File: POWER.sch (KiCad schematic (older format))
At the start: 35 parts, among them U201 TPS61021A, U402 MAX1555

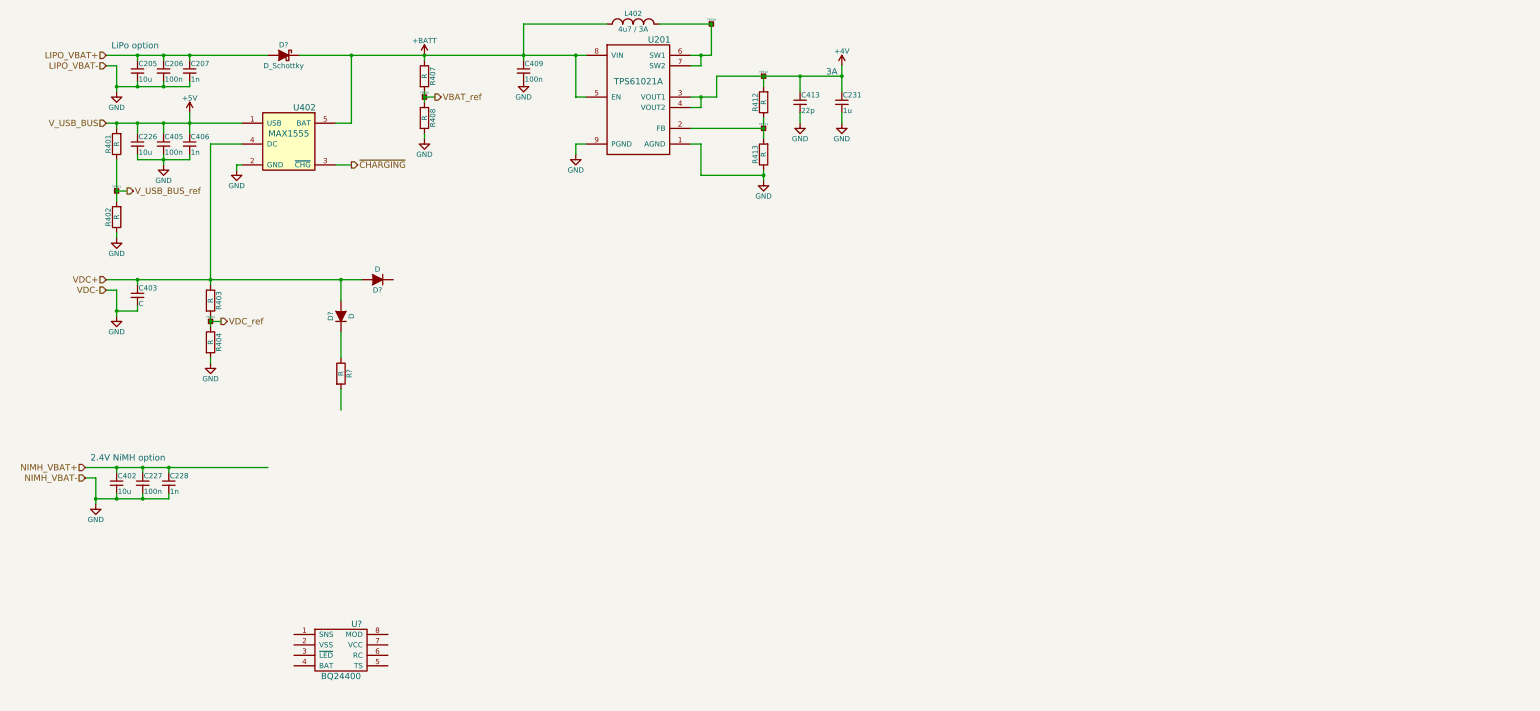
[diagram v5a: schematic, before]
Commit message: Added power domains overview in POWER.sch subsheet fixed some power connections added datasheet for bq24401 charge controller updated schematic library
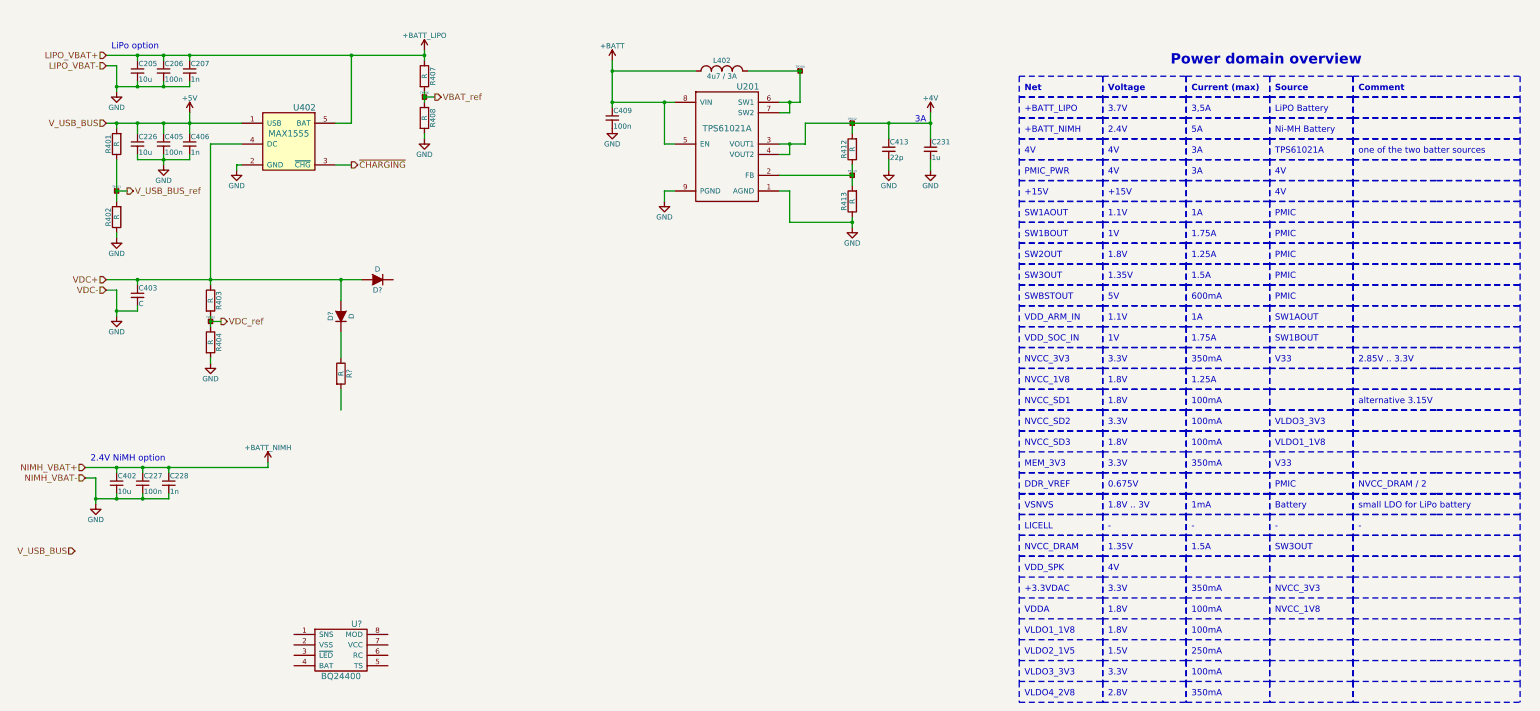
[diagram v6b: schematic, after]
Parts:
- removed D?: D_Schottky, symbol D_Schottky
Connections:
- net +BATT: no longer R407.1, U402.5 (BAT)
- net LIPO_VBAT+ renamed +BATT_LIPO
- net +BATT_LIPO: now also R407.1, U402.5 (BAT)
- net NIMH_VBAT+ renamed +BATT_NIMH
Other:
- note added: "+15V"
- note added: "+3.3VDAC"
- note added: "+BATT_LIPO"
- note added: "+BATT_NIMH"
- note added: "-"
- note added: "0.675V"
- note added: "1.1V"
- note added: "1.25A"
- note added: "1.35V"
- note added: "1.5A"
- note added: "1.5V"
- note added: "1.75A"
- note added: "1.8V"
- note added: "1.8V .. 3V"
- note added: "100mA"
- note added: "1A"
- note added: "1V"
- note added: "1mA"
- note added: "2.4V"
- note added: "2.85V .. 3.3V"
- note added: "2.8V"
- note added: "250mA"
- note added: "3,5A"
- note added: "3.3V"
- note added: "3.7V"
- note added: "350mA"
- note added: "4V"
- note added: "5A"
- note added: "5V"
- note added: "600mA"
- note added: "Battery"
- note added: "Comment"
- note added: "Current (max)"
- note added: "DDR_VREF"
- note added: "LICELL"
- note added: "LiPO Battery"
- note added: "MEM_3V3"
- note added: "NVCC_1V8"
- note added: "NVCC_3V3"
- note added: "NVCC_DRAM"
- note added: "NVCC_DRAM / 2"
- note added: "NVCC_SD1"
- note added: "NVCC_SD2"
- note added: "NVCC_SD3"
- note added: "Net"
- note added: "Ni-MH Battery"
- note added: "PMIC"
- note added: "PMIC_PWR"
- note added: "Power domain overview"
- note added: "SW1AOUT"
- note added: "SW1BOUT"
- note added: "SW2OUT"
- note added: "SW3OUT"
- note added: "SWBSTOUT"
- note added: "Source"
- note added: "TPS61021A"
- note added: "V33"
- note added: "VDDA"
- note added: "VDD_ARM_IN"
- note added: "VDD_SOC_IN"
- note added: "VDD_SPK"
- note added: "VLDO1_1V8"
- note added: "VLDO2_1V5"
- note added: "VLDO3_3V3"
- note added: "VLDO4_2V8"
- note added: "VSNVS"
- note added: "Voltage"
- note added: "alternative 3.15V"
- note added: "one of the two batter sources"
- note added: "small LDO for LiPo battery"
- moved on the sheet: C231, C409, C413, L402, R412, R413, TP209, TP212, TP213, U201

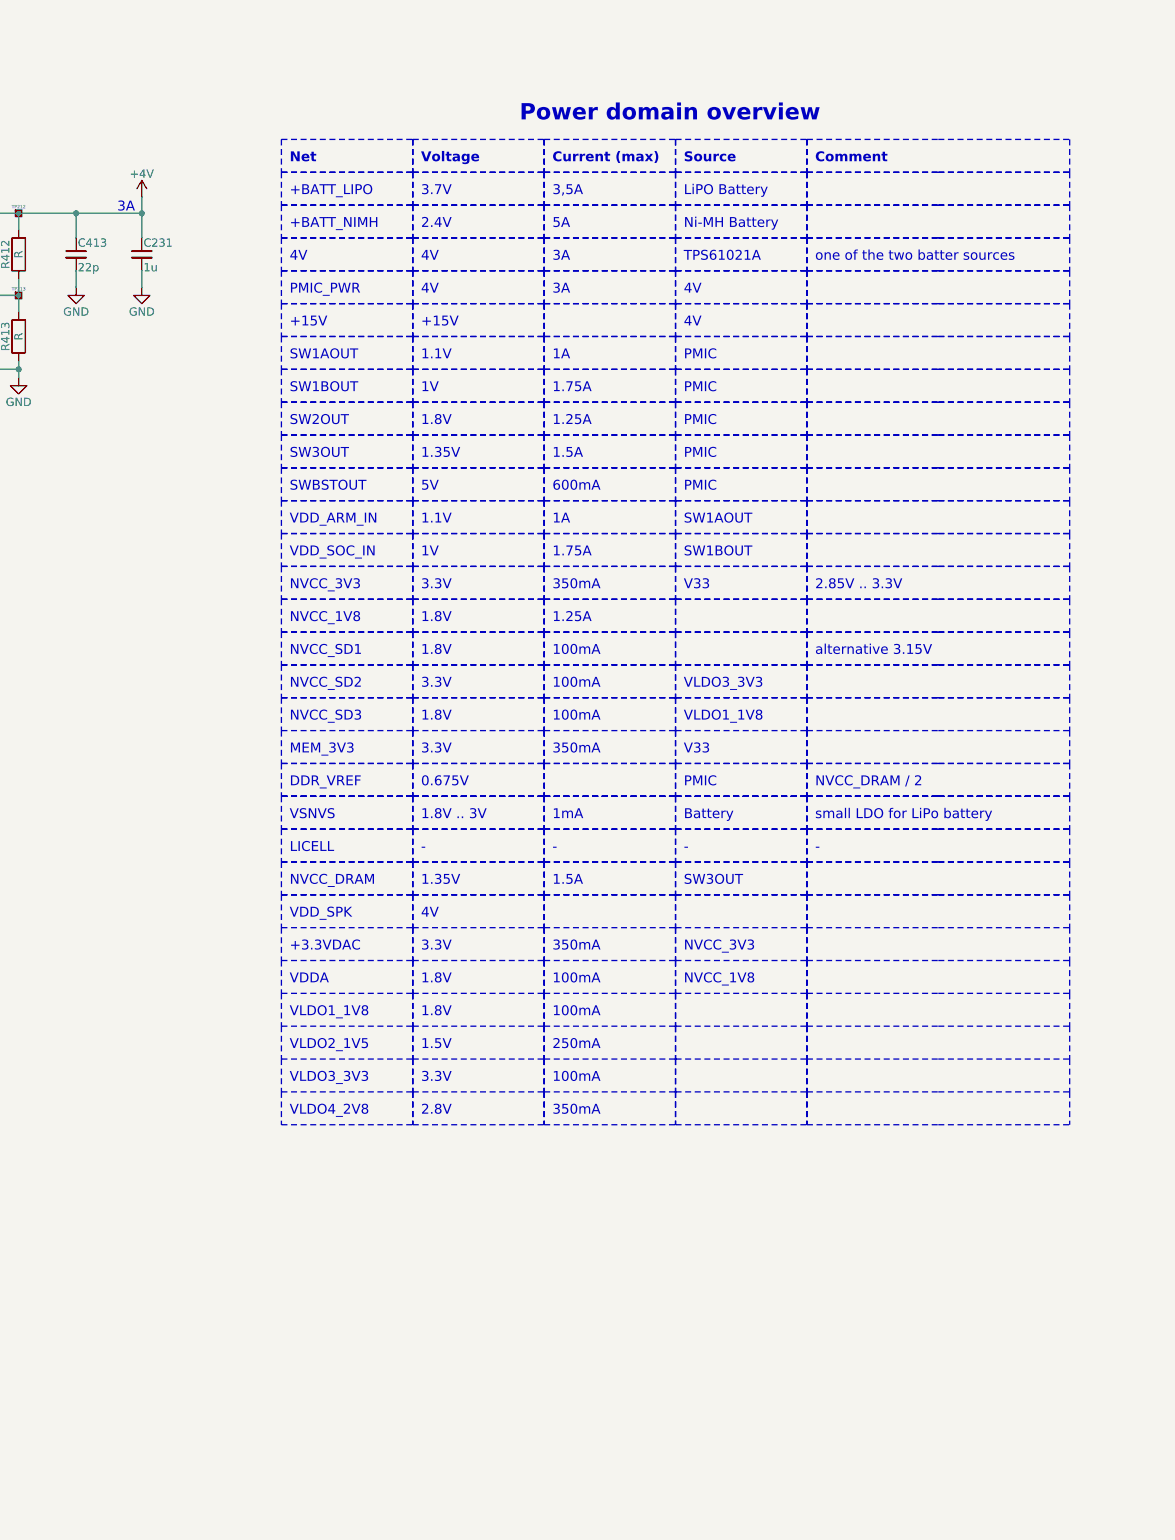
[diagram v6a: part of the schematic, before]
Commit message: Modified power domain overview to contain tree of power rails updated schematic lib reference
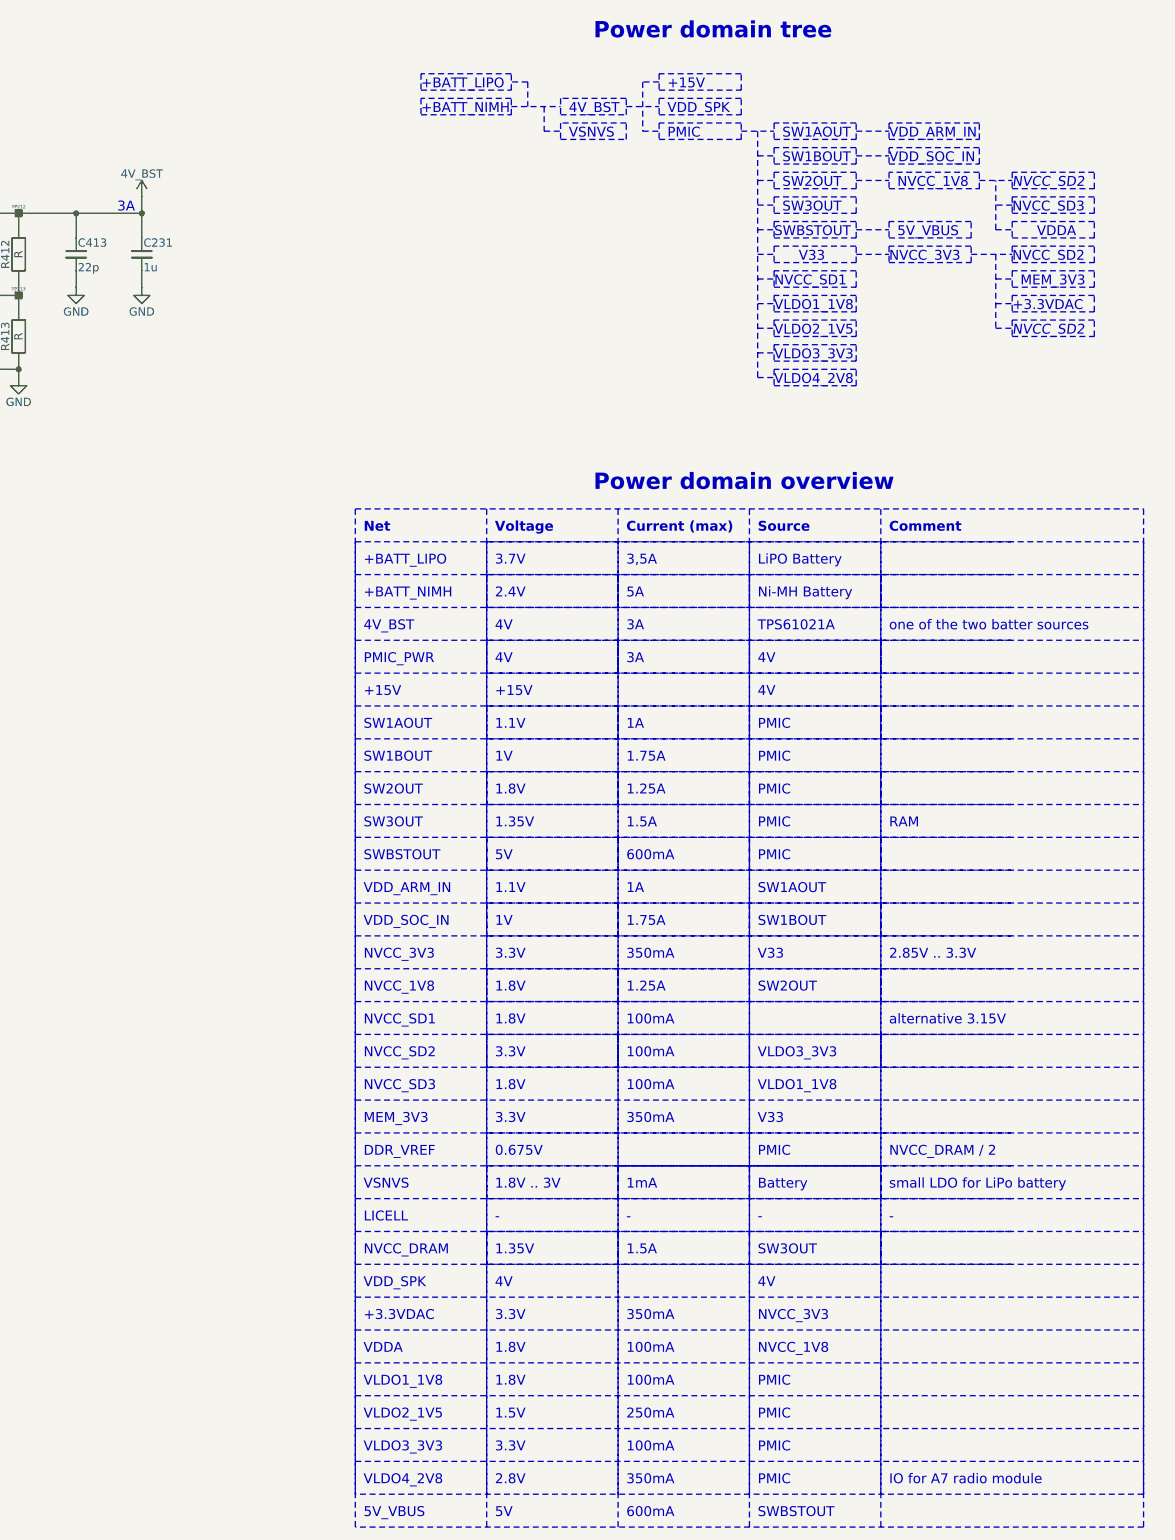
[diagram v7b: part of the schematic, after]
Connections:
- net +4V renamed 4V_BST
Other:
- note added: "4V_BST"
- note added: "5V_VBUS"
- note added: "IO for A7 radio module"
- note added: "Power domain tree"
- note added: "RAM"
